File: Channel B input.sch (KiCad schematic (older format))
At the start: 21 parts, among them J1 MJ-3523-SMT-TR, J10 Conn_01x10, J5 Conn_01x02, P1 100k, SW1 SW_SPDT, U1 TL072

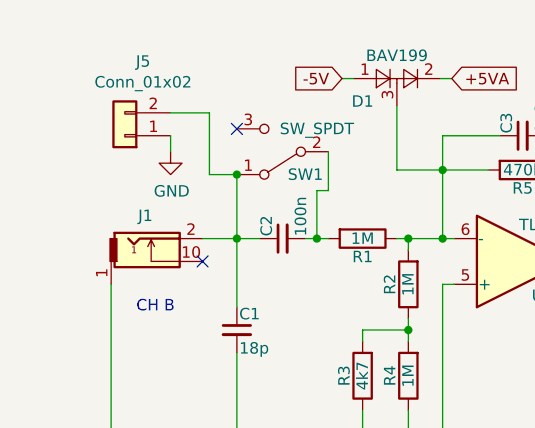
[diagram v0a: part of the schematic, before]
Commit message: fixed schematic and updated PCB
Fixed the schematic after having found the issues in the GBDSO schematic (which is also fixed on the repo).
Continued making the PCB for the modules. We're not at 7 modules from 10.
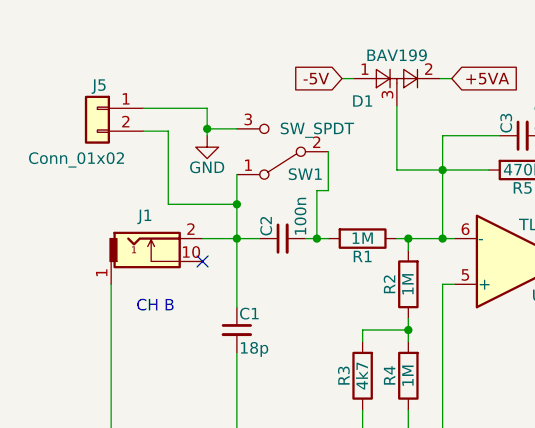
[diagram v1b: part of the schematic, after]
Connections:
- net GND: now also SW1.3 (C)
- no-connect marks 3 -> 2
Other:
- moved on the sheet: J5
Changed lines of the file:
@@
 	1990 1800 2040 1800
 Wire Wire Line
-	1640 1520 1640 1800
+	1640 1520 1640 1650
 Wire Wire Line
 	6030 1360 6030 1300
@@
 Wire Wire Line
 	5050 1900 5300 1900
-NoConn ~ 1640 1320
 $Comp
 L Connector_Generic:Conn_01x02 J?
 U 1 1 5F84E74B
-P 1150 1350
+P 1030 1230
 AR Path="/5F84E74B" Ref="J?"  Part="1"
 AR Path="/5F6C55C3/5F84E74B" Ref="J?"  Part="1"
 AR Path="/5F6C72AE/5F84E74B" Ref="J5"  Part="1"
-F 0 "J5" H 1070 1025 50  0000 C CNN
-F 1 "Conn_01x02" H 1070 1116 50  0000 C CNN
-F 2 "Connector_PinHeader_2.54mm:PinHeader_1x02_P2.54mm_Horizontal" H 1150 1350 50  0001 C CNN
-F 3 "~" H 1150 1350 50  0001 C CNN
-	1    1150 1350
-	-1   0    0    1
-$EndComp
-Wire Wire Line
-	1350 1250 1520 1250
-Wire Wire Line
-	1520 1250 1520 1520
-Wire Wire Line
-	1520 1520 1640 1520
-Connection ~ 1640 1520
+F 0 "J5" H 1020 1330 50  0000 C CNN
+F 1 "Conn_01x02" H 1120 1010 50  0000 C CNN
+F 2 "Connector_PinHeader_2.54mm:PinHeader_1x02_P2.54mm_Horizontal" H 1030 1230 50  0001 C CNN
+F 3 "~" H 1030 1230 50  0001 C CNN
+	1    1030 1230
+	-1   0    0    -1
+$EndComp
 $Comp
 L power:GND #PWR?
 U 1 1 5F84E755
-P 1350 1420
+P 1510 1350
 AR Path="/5F6C55C3/5F84E755" Ref="#PWR?"  Part="1"
 AR Path="/5F6C72AE/5F84E755" Ref="#PWR0104"  Part="1"
-F 0 "#PWR0104" H 1350 1170 50  0001 C CNN
-F 1 "GND" H 1355 1247 50  0000 C CNN
-F 2 "" H 1350 1420 50  0001 C CNN
-F 3 "" H 1350 1420 50  0001 C CNN
-	1    1350 1420
-	1    0    0    -1
-$EndComp
-Wire Wire Line
-	1350 1350 1350 1420
+F 0 "#PWR0104" H 1510 1100 50  0001 C CNN
+F 1 "GND" H 1510 1210 50  0000 C CNN
+F 2 "" H 1510 1350 50  0001 C CNN
+F 3 "" H 1510 1350 50  0001 C CNN
+	1    1510 1350
+	1    0    0    -1
+$EndComp
 Text Notes 1200 2130 0    50   ~ 0
 CH B
@@
 -2.5V
 NoConn ~ 4040 3930
+Wire Wire Line
+	1510 1350 1510 1320
+Wire Wire Line
+	1510 1320 1640 1320
+Wire Wire Line
+	1230 1230 1510 1230
+Wire Wire Line
+	1510 1230 1510 1320
+Connection ~ 1510 1320
+Wire Wire Line
+	1640 1650 1340 1650
+Wire Wire Line
+	1340 1650 1340 1330
+Wire Wire Line
+	1340 1330 1230 1330
+Connection ~ 1640 1650
+Wire Wire Line
+	1640 1650 1640 1800
 $EndSCHEMATC
